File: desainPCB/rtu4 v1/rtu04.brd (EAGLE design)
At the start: 78.7 x 77.1 mm, 17 parts, among them M1 ARDUINO-PRO-MINI-5.0V, X1 JST-XH-02-PIN-LONG-PAD

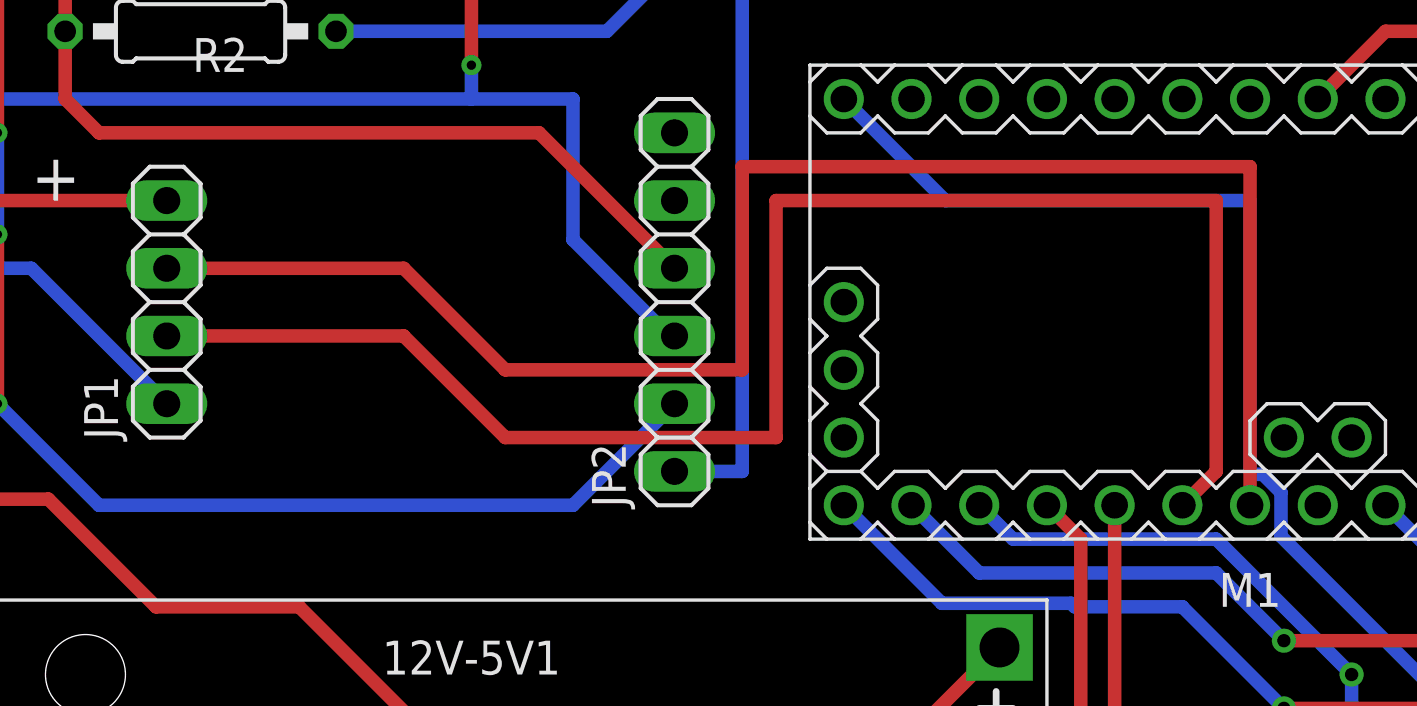
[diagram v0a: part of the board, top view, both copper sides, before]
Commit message: fix calib for strain 2.0
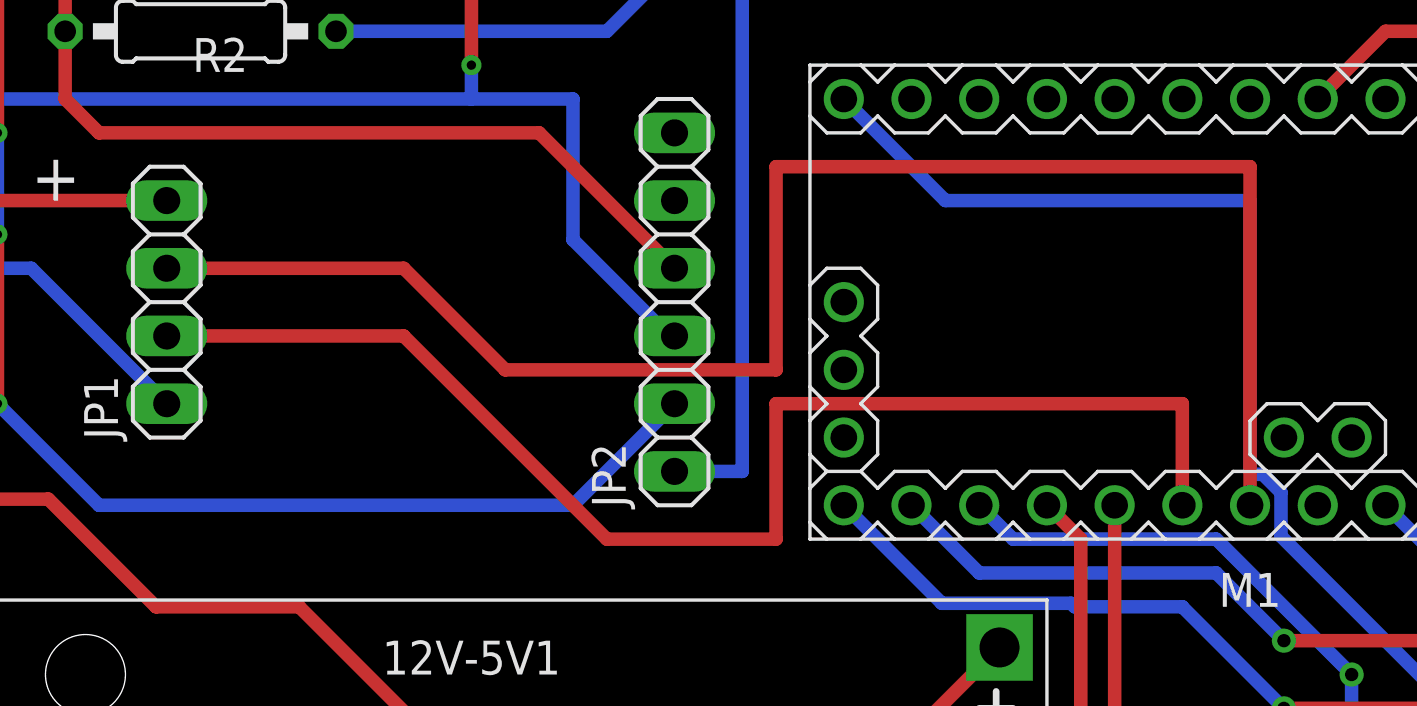
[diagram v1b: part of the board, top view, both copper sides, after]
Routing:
- net A1: track 61.8 -> 50.1 mm
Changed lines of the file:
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@@
 <signal name="A1">
 <contactref element="M1" pad="J6.7"/>
-<wire x1="30.48" y1="50.8" x2="26.67" y2="54.61" width="0.508" layer="1"/>
-<wire x1="30.48" y1="50.8" x2="40.64" y2="50.8" width="0.508" layer="1"/>
-<wire x1="40.64" y1="50.8" x2="40.64" y2="59.69" width="0.508" layer="1"/>
-<wire x1="40.64" y1="59.69" x2="57.15" y2="59.69" width="0.508" layer="1"/>
-<wire x1="57.15" y1="59.69" x2="57.15" y2="49.53" width="0.508" layer="1"/>
-<wire x1="57.15" y1="49.53" x2="55.88" y2="48.26" width="0.508" layer="1"/>
 <contactref element="JP1" pad="2"/>
-<wire x1="26.67" y1="54.61" x2="17.78" y2="54.61" width="0.508" layer="1"/>
+<wire x1="17.78" y1="54.61" x2="26.67" y2="54.61" width="0.508" layer="1"/>
+<wire x1="40.64" y1="46.99" x2="40.64" y2="52.07" width="0.508" layer="1"/>
+<wire x1="40.64" y1="52.07" x2="55.88" y2="52.07" width="0.508" layer="1"/>
+<wire x1="55.88" y1="52.07" x2="55.88" y2="48.26" width="0.508" layer="1"/>
+<wire x1="26.67" y1="54.61" x2="34.29" y2="46.99" width="0.508" layer="1"/>
+<wire x1="34.29" y1="46.99" x2="40.64" y2="46.99" width="0.508" layer="1"/>
 </signal>
 <signal name="10">
@@
 <contactref element="M1" pad="J6.6"/>
 <wire x1="30.48" y1="53.34" x2="26.67" y2="57.15" width="0.508" layer="1"/>
-<wire x1="30.48" y1="53.34" x2="39.37" y2="53.34" width="0.508" layer="1"/>
-<wire x1="39.37" y1="53.34" x2="39.37" y2="60.96" width="0.508" layer="1"/>
-<wire x1="39.37" y1="60.96" x2="58.42" y2="60.96" width="0.508" layer="1"/>
+<wire x1="30.48" y1="53.34" x2="40.64" y2="53.34" width="0.508" layer="1"/>
+<wire x1="40.64" y1="53.34" x2="40.64" y2="60.96" width="0.508" layer="1"/>
+<wire x1="40.64" y1="60.96" x2="58.42" y2="60.96" width="0.508" layer="1"/>
 <wire x1="58.42" y1="60.96" x2="58.42" y2="48.26" width="0.508" layer="1"/>
 <contactref element="JP1" pad="3"/>
